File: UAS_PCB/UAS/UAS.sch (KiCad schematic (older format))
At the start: 17 parts, among them J1 SM02B-PASS-TBT, J2 SM02B-PASS-TBT, J3 SM02B-PASS-TBT, J4 SM02B-PASS-TBT, U1 JST-7-Pin, U10 UAS-rescue_7.5V-2.4A-Converte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, U11 JST-3-Pin, U2 5A-5V-Converter, U3 500mA-5V-Converter, U4 12V-StepUp-Converter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

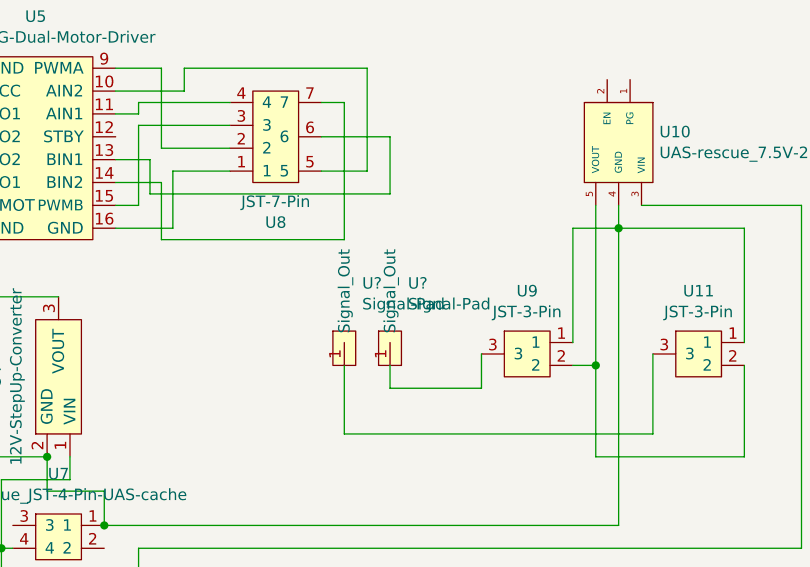
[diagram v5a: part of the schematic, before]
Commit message: footpirnt placement changes, need room for traces
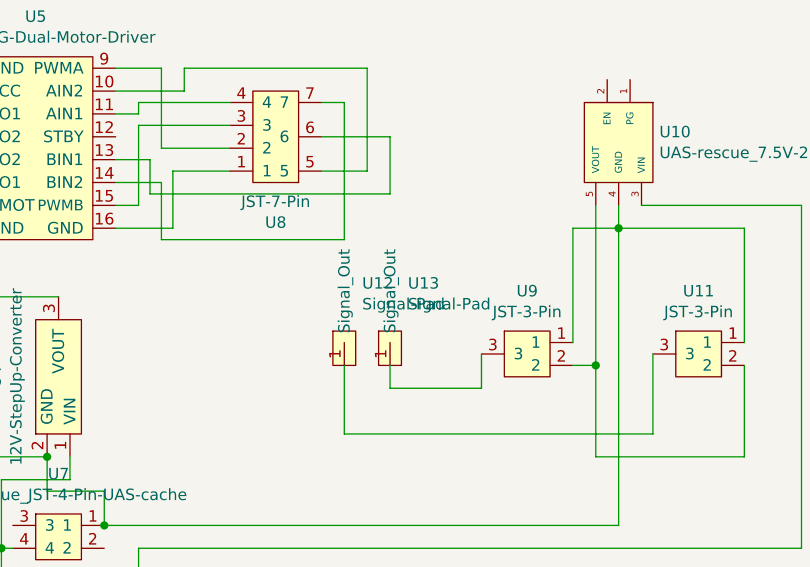
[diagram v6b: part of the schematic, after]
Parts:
- gave numbers to parts that had none: 2
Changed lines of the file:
@@
 Connection ~ 2900 3250
 $Comp
-L UAS-rescue:Signal-Pad-UAS-cache U?
+L UAS-rescue:Signal-Pad-UAS-cache U12
 U 1 1 60391DEE
 P 4250 5500
-F 0 "U?" H 4328 5759 50  0000 L CNN
+F 0 "U12" H 4328 5759 50  0000 L CNN
 F 1 "Signal-Pad" H 4328 5668 50  0000 L CNN
 F 2 "UAS:Individual_Solder_Pad" H 4250 5500 50  0001 C CNN
@@
 $EndComp
 $Comp
-L UAS-rescue:Signal-Pad-UAS-cache U?
+L UAS-rescue:Signal-Pad-UAS-cache U13
 U 1 1 60392D35
 P 4450 5500
-F 0 "U?" H 4528 5759 50  0000 L CNN
+F 0 "U13" H 4528 5759 50  0000 L CNN
 F 1 "Signal-Pad" H 4528 5668 50  0000 L CNN
 F 2 "UAS:Individual_Solder_Pad" H 4450 5500 50  0001 C CNN

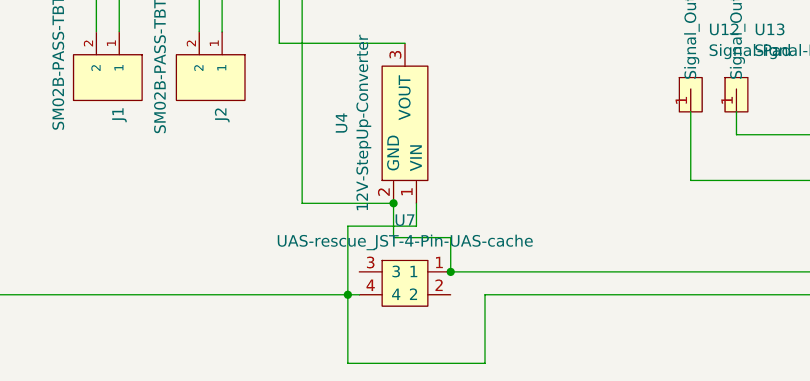
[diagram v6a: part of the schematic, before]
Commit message: fixed courtyard errors
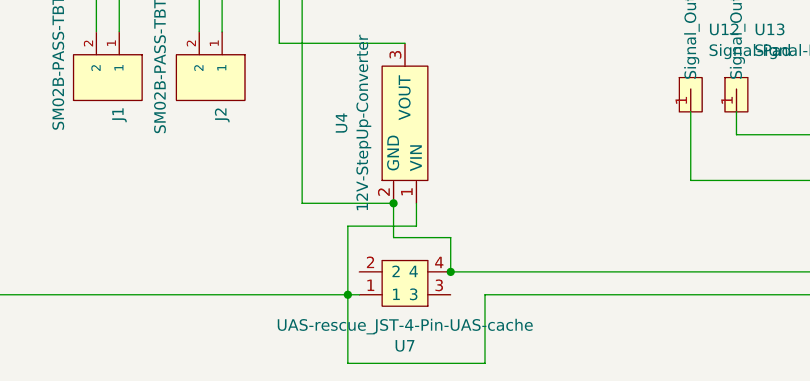
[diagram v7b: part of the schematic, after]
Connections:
- net at U10.3 (VIN), U2.2 (VIN), U3.2 (VIN)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: now also U7.1; no longer U7.4
- net at U10.4 (GND), U11.1, U2.4 (GND)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: now also U7.4; no longer U7.1
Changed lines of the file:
@@
 L UAS-rescue:UAS-rescue_JST-4-Pin-UAS-cache-UAS-cache U7
 U 1 1 6037EE1D
-P 3000 6150
-F 0 "U7" H 3000 6225 50  0000 C CNN
-F 1 "UAS-rescue_JST-4-Pin-UAS-cache" H 3000 6134 50  0000 C CNN
-F 2 "UAS:JST_XH_B4B-XH-A_1x04_P2.50mm_Vertical" H 3000 6250 50  0001 C CNN
-F 3 "" H 3000 6250 50  0001 C CNN
-	1    3000 6150
-	1    0    0    -1
+P 3000 6550
+F 0 "U7" H 3000 6625 50  0000 C CNN
+F 1 "UAS-rescue_JST-4-Pin-UAS-cache" H 3000 6534 50  0000 C CNN
+F 2 "UAS:JST_XH_B4B-XH-A_1x04_P2.50mm_Vertical" H 3000 6650 50  0001 C CNN
+F 3 "" H 3000 6650 50  0001 C CNN
+	1    3000 6550
+	-1   0    0    1
 $EndComp
 Wire Wire Line

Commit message: First traces
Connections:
- net GND: now reaches U10.4 (GND), U11.1, U2.4 (GND), U4.2 (GND), U5.8 (GND), U7.4, U9.1
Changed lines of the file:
@@
 Wire Wire Line
 	4450 5700 4450 5600
+$Comp
+L power:GND #PWR?
+U 1 1 6038ECCA
+P 3200 6150
+F 0 "#PWR?" H 3200 5900 50  0001 C CNN
+F 1 "GND" H 3205 5977 50  0000 C CNN
+F 2 "" H 3200 6150 50  0001 C CNN
+F 3 "" H 3200 6150 50  0001 C CNN
+	1    3200 6150
+	-1   0    0    1
+$EndComp
+Connection ~ 3200 6150
 $EndSCHEMATC
